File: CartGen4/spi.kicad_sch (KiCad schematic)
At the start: 11 parts, among them J1 MEM2080-00-128-00-A, U10 IS25WP080D-JNLE, U11 DS1391U-33+, Y1 FC-135R 32.7680KA-E5

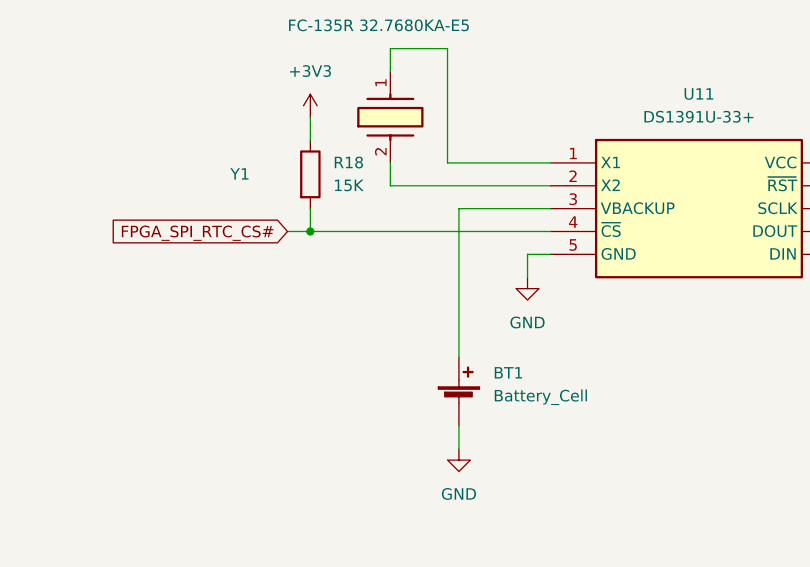
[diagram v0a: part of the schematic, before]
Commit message: Wired SPI bus
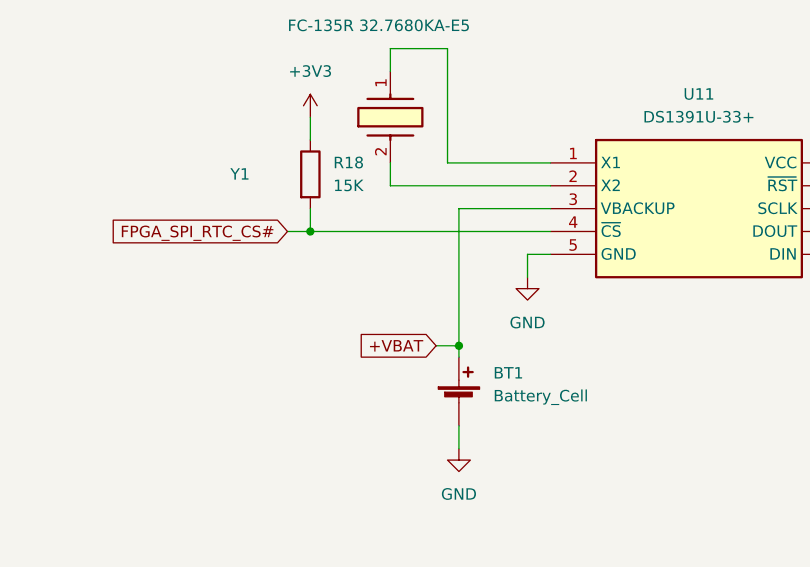
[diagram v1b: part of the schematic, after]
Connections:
- net +VBAT: now reaches BT1.1 (+), U11.3 (VBACKUP)
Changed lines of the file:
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@@
   (junction (at 66.04 125.73) (diameter 0) (color 0 0 0 0)
+  )
+  (junction (at 184.15 88.9) (diameter 0) (color 0 0 0 0)
   )
   (junction (at 252.73 68.58) (diameter 0) (color 0 0 0 0)
@@
     (stroke (width 0) (type default) (color 0 0 0 0))
   )
-  (wire (pts (xy 184.15 90.17) (xy 184.15 73.66))
+  (wire (pts (xy 184.15 90.17) (xy 184.15 88.9))
     (stroke (width 0) (type default) (color 0 0 0 0))
   )
@@
     (stroke (width 0) (type default) (color 0 0 0 0))
   )
+  (wire (pts (xy 184.15 88.9) (xy 184.15 73.66))
+    (stroke (width 0) (type default) (color 0 0 0 0))
+  )
   (wire (pts (xy 118.11 69.85) (xy 118.11 67.31))
+    (stroke (width 0) (type default) (color 0 0 0 0))
+  )
+  (wire (pts (xy 181.61 88.9) (xy 184.15 88.9))
     (stroke (width 0) (type default) (color 0 0 0 0))
   )
@@
       (effects (font (size 1.27 1.27)) (justify right) hide)
     )
+  )
+  (global_label "+VBAT" (shape input) (at 181.61 88.9 180) (fields_autoplaced)
+    (effects (font (size 1.27 1.27)) (justify right))
+    (property "Intersheet References" "${INTERSHEET_REFS}" (id 0) (at 173.2098 88.8206 0)
+      (effects (font (size 1.27 1.27)) (justify right) hide)
+    )

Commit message: Updated field information
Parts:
- BT1: MFN (none) -> Keystone Electronics; MFP (none) -> 2894; Notes Battery is utilised and maintained by the DS1391U-33+ RTC. -> Battery is utilised and maintained by the DS1391U-33+ RTC. 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
- C33, C34, C35: Package ID (none) -> 0402
- J1: Notes (none) -> SD card connector; Source (none) -> SPEC
- R16, R17, R18: Notes (none) -> Pullup resistor for ensuring that slave is not selecting du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; Package ID (none) -> 0402
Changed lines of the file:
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@@
+      (effects (font (size 1.27 1.27)) hide)
+    )
+    (property "Notes" "Pullup resistor for ensuring that slave is not selecting during startup" (id 7) (at 167.64 69.85 0)
+      (effects (font (size 1.27 1.27)) hide)
+    )
+    (property "Description" "~" (id 8) (at 167.64 69.85 0)
+      (effects (font (size 1.27 1.27)) hide)
+    )
+    (property "MFN" "~" (id 9) (at 167.64 69.85 0)
+      (effects (font (size 1.27 1.27)) hide)
+    )
+    (property "MFP" "~" (id 10) (at 167.64 69.85 0)
+      (effects (font (size 1.27 1.27)) hide)
+    )
+    (property "Package ID" "0402" (id 11) (at 167.64 69.85 0)
       (effects (font (size 1.27 1.27)) hide)
     )
@@
     )
     (property "MFP" "MEM2080-00-128-00-A" (id 7) (at 87.63 132.08 0)
+      (effects (font (size 1.27 1.27)) hide)
+    )
+    (property "Notes" "SD card connector" (id 8) (at 87.63 132.08 0)
+      (effects (font (size 1.27 1.27)) hide)
+    )
+    (property "Package ID" "~" (id 9) (at 87.63 132.08 0)
+      (effects (font (size 1.27 1.27)) hide)
+    )
+    (property "Source" "SPEC" (id 10) (at 87.63 132.08 0)
       (effects (font (size 1.27 1.27)) hide)
     )
@@
       (effects (font (size 1.27 1.27)) hide)
     )
+    (property "Description" "~" (id 7) (at 118.11 76.2 0)
+      (effects (font (size 1.27 1.27)) hide)
+    )
+    (property "MFN" "~" (id 8) (at 118.11 76.2 0)
+      (effects (font (size 1.27 1.27)) hide)
+    )
+    (property "MFP" "~" (id 9) (at 118.11 76.2 0)
+      (effects (font (size 1.27 1.27)) hide)
+    )
+    (property "Package ID" "0402" (id 10) (at 118.11 76.2 0)
+      (effects (font (size 1.27 1.27)) hide)
+    )
     (pin "1")
     (pin "2")
@@
     )
     (property "Source" "ANY" (id 6) (at 58.42 132.08 0)
+      (effects (font (size 1.27 1.27)) hide)
+    )
+    (property "Description" "~" (id 7) (at 58.42 132.08 0)
+      (effects (font (size 1.27 1.27)) hide)
+    )
+    (property "MFN" "~" (id 8) (at 58.42 132.08 0)
+      (effects (font (size 1.27 1.27)) hide)
+    )
+    (property "MFP" "~" (id 9) (at 58.42 132.08 0)
+      (effects (font (size 1.27 1.27)) hide)
+    )
+    (property "Package ID" "0402" (id 10) (at 58.42 132.08 0)
       (effects (font (size 1.27 1.27)) hide)
     )
@@
       (effects (font (size 1.27 1.27)) hide)
     )
+    (property "Notes" "Pullup resistor for ensuring that slave is not selecting during startup" (id 7) (at 45.72 139.7 0)
+      (effects (font (size 1.27 1.27)) hide)
+    )
+    (property "Description" "~" (id 8) (at 45.72 139.7 0)
+      (effects (font (size 1.27 1.27)) hide)
+    )
+    (property "MFN" "~" (id 9) (at 45.72 139.7 0)
+      (effects (font (size 1.27 1.27)) hide)
+    )
+    (property "MFP" "~" (id 10) (at 45.72 139.7 0)
+      (effects (font (size 1.27 1.27)) hide)
+    )
+    (property "Package ID" "0402" (id 11) (at 45.72 139.7 0)
+      (effects (font (size 1.27 1.27)) hide)
+    )
     (pin "1")
     (pin "2")
@@
     )
     (property "Source" "ANY" (id 6) (at 252.73 74.93 0)
+      (effects (font (size 1.27 1.27)) hide)
+    )
+    (property "Description" "~" (id 7) (at 252.73 74.93 0)
+      (effects (font (size 1.27 1.27)) hide)
+    )
+    (property "MFN" "~" (id 8) (at 252.73 74.93 0)
+      (effects (font (size 1.27 1.27)) hide)
+    )
+    (property "MFP" "~" (id 9) (at 252.73 74.93 0)
+      (effects (font (size 1.27 1.27)) hide)
+    )
+    (property "Package ID" "0402" (id 10) (at 252.73 74.93 0)
       (effects (font (size 1.27 1.27)) hide)
     )
@@
       (effects (font (size 1.27 1.27)) hide)
     )
-    (property "Datasheet" "~" (id 3) (at 184.15 93.726 90)
+    (property "Datasheet" "https://nl.mouser.com/datasheet/2/215/Keystone_Electronics_04082019_2894-1551346.pdf" (id 3) (at 184.15 93.726 90)
       (effects (font (size 1.27 1.27)) hide)
     )
@@
       (effects (font (size 1.27 1.27)) hide)
     )
-    (property "Notes" "Battery is utilised and maintained by the DS1391U-33+ RTC." (id 5) (at 184.15 95.25 0)
+    (property "Notes" "Battery is utilised and maintained by the DS1391U-33+ RTC. Be sure to disable charging when using non-rechargable batteries." (id 5) (at 184.15 95.25 0)
       (effects (font (size 1.27 1.27)) hide)
     )
     (property "Source" "SPEC" (id 6) (at 184.15 95.25 0)
+      (effects (font (size 1.27 1.27)) hide)
+    )
+    (property "Description" "CR2025 battery holder" (id 7) (at 184.15 95.25 0)
+      (effects (font (size 1.27 1.27)) hide)
+    )
+    (property "MFN" "Keystone Electronics" (id 8) (at 184.15 95.25 0)
+      (effects (font (size 1.27 1.27)) hide)
+    )
+    (property "MFP" "2894" (id 9) (at 184.15 95.25 0)
+      (effects (font (size 1.27 1.27)) hide)
+    )
+    (property "Package ID" "~" (id 10) (at 184.15 95.25 0)
       (effects (font (size 1.27 1.27)) hide)
     )
@@
       (effects (font (size 1.27 1.27)) hide)
     )
+    (property "Notes" "Pullup resistor for ensuring that slave is not selecting during startup" (id 7) (at 54.61 63.5 0)
+      (effects (font (size 1.27 1.27)) hide)
+    )
+    (property "Description" "~" (id 8) (at 54.61 63.5 0)
+      (effects (font (size 1.27 1.27)) hide)
+    )
+    (property "MFN" "~" (id 9) (at 54.61 63.5 0)
+      (effects (font (size 1.27 1.27)) hide)
+    )
+    (property "MFP" "~" (id 10) (at 54.61 63.5 0)
+      (effects (font (size 1.27 1.27)) hide)
+    )
+    (property "Package ID" "0402" (id 11) (at 54.61 63.5 0)
+      (effects (font (size 1.27 1.27)) hide)
+    )

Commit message: Updated some component fields
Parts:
- BT1: Supplier suggestion (none) -> https://nl.mouser.com/ProductDetail/Keystone-Electronics/28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
- C33, C34, C35: Supplier suggestion (none) -> https://nl.mouser.com/ProductDetail/Murata-Electronics/GRM1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; Tolerance (none) -> 20%; Voltage (none) -> 3V3
- J1: Supplier suggestion (none) -> https://nl.mouser.com/ProductDetail/GCT/MEM2080-00-128-00-A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
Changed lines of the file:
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@@
+      (effects (font (size 1.27 1.27)) hide)
+    )
+    (property "Supplier suggestion" "https://nl.mouser.com/ProductDetail/GCT/MEM2080-00-128-00-A?qs=vvQtp7zwQdPJXzpf1SnYug%3D%3D" (id 11) (at 87.63 132.08 0)
       (effects (font (size 1.27 1.27)) hide)
     )
@@
       (effects (font (size 1.27 1.27)) hide)
     )
+    (property "Supplier suggestion" "https://nl.mouser.com/ProductDetail/Murata-Electronics/GRM155R61C104KA88J?qs=sGAEpiMZZMsh%252B1woXyUXj8YF%2FGivH5Kx4uStnYyl8jU%3D" (id 11) (at 118.11 76.2 0)
+      (effects (font (size 1.27 1.27)) hide)
+    )
+    (property "Tolerance" "20%" (id 12) (at 118.11 76.2 0)
+      (effects (font (size 1.27 1.27)) hide)
+    )
+    (property "Voltage" "3V3" (id 13) (at 118.11 76.2 0)
+      (effects (font (size 1.27 1.27)) hide)
+    )
     (pin "1")
     (pin "2")
@@
     )
     (property "Package ID" "0402" (id 10) (at 58.42 132.08 0)
+      (effects (font (size 1.27 1.27)) hide)
+    )
+    (property "Supplier suggestion" "https://nl.mouser.com/ProductDetail/Murata-Electronics/GRM155R61C104KA88J?qs=sGAEpiMZZMsh%252B1woXyUXj8YF%2FGivH5Kx4uStnYyl8jU%3D" (id 11) (at 58.42 132.08 0)
+      (effects (font (size 1.27 1.27)) hide)
+    )
+    (property "Tolerance" "20%" (id 12) (at 58.42 132.08 0)
+      (effects (font (size 1.27 1.27)) hide)
+    )
+    (property "Voltage" "3V3" (id 13) (at 58.42 132.08 0)
       (effects (font (size 1.27 1.27)) hide)
     )
@@
     )
     (property "Package ID" "0402" (id 10) (at 252.73 74.93 0)
+      (effects (font (size 1.27 1.27)) hide)
+    )
+    (property "Supplier suggestion" "https://nl.mouser.com/ProductDetail/Murata-Electronics/GRM155R61C104KA88J?qs=sGAEpiMZZMsh%252B1woXyUXj8YF%2FGivH5Kx4uStnYyl8jU%3D" (id 11) (at 252.73 74.93 0)
+      (effects (font (size 1.27 1.27)) hide)
+    )
+    (property "Tolerance" "20%" (id 12) (at 252.73 74.93 0)
+      (effects (font (size 1.27 1.27)) hide)
+    )
+    (property "Voltage" "3V3" (id 13) (at 252.73 74.93 0)
       (effects (font (size 1.27 1.27)) hide)
     )
@@
       (effects (font (size 1.27 1.27)) hide)
     )
+    (property "Supplier suggestion" "https://nl.mouser.com/ProductDetail/Keystone-Electronics/2894?qs=u16ybLDytRb94n%2F3dXyVLQ%3D%3D" (id 11) (at 184.15 95.25 0)
+      (effects (font (size 1.27 1.27)) hide)
+    )

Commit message: Added missing recommendations
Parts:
- R16, R17, R18: Supplier suggestion (none) -> https://nl.mouser.com/ProductDetail/Kamaya/RMC1-16S-153JTH?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
- U10: Supplier suggestion (none) -> https://nl.mouser.com/ProductDetail/ISSI/IS25WP080D-JNLE?qs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
- U11: Supplier suggestion (none) -> https://nl.mouser.com/ProductDetail/Analog-Devices-Maxim-In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
- Y1: Supplier suggestion (none) -> https://nl.mouser.com/ProductDetail/Epson-Timing/FC-135R-32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
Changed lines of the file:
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@@
+      (effects (font (size 1.27 1.27)) hide)
+    )
+    (property "Supplier suggestion" "https://nl.mouser.com/ProductDetail/Kamaya/RMC1-16S-153JTH?qs=sGAEpiMZZMvdGkrng054t%252BjmMOhbS7JJ11bN0iqZRdOn%2Fu9rqH1%2FEw%3D%3D" (id 12) (at 167.64 69.85 0)
       (effects (font (size 1.27 1.27)) hide)
     )
@@
       (effects (font (size 1.27 1.27)) hide)
     )
+    (property "Supplier suggestion" "https://nl.mouser.com/ProductDetail/Epson-Timing/FC-135R-32.7680KA-E5?qs=%252B6g0mu59x7IiWErQB8ij2w%3D%3D" (id 18) (at 176.53 68.58 0)
+      (effects (font (size 1.27 1.27)) hide)
+    )
     (pin "1")
     (pin "2")
@@
     )
     (property "Package ID" "0402" (id 11) (at 45.72 139.7 0)
+      (effects (font (size 1.27 1.27)) hide)
+    )
+    (property "Supplier suggestion" "https://nl.mouser.com/ProductDetail/Kamaya/RMC1-16S-153JTH?qs=sGAEpiMZZMvdGkrng054t%252BjmMOhbS7JJ11bN0iqZRdOn%2Fu9rqH1%2FEw%3D%3D" (id 12) (at 45.72 139.7 0)
       (effects (font (size 1.27 1.27)) hide)
     )
@@
     )
     (property "Package ID" "SOIC-8" (id 10) (at 67.31 69.85 0)
+      (effects (font (size 1.27 1.27)) hide)
+    )
+    (property "Supplier suggestion" "https://nl.mouser.com/ProductDetail/ISSI/IS25WP080D-JNLE?qs=pif5%252B9MYt0UdCheWbE26RA%3D%3D" (id 11) (at 67.31 69.85 0)
       (effects (font (size 1.27 1.27)) hide)
     )
@@
     )
     (property "Source" "SPEC" (id 10) (at 194.31 68.58 0)
+      (effects (font (size 1.27 1.27)) hide)
+    )
+    (property "Supplier suggestion" "https://nl.mouser.com/ProductDetail/Analog-Devices-Maxim-Integrated/DS1391U-33%2b?qs=0Y9aZN%252BMVCVmg1eZRkyk7Q%3D%3D" (id 11) (at 194.31 68.58 0)
       (effects (font (size 1.27 1.27)) hide)
     )
@@
       (effects (font (size 1.27 1.27)) hide)
     )
+    (property "Supplier suggestion" "https://nl.mouser.com/ProductDetail/Kamaya/RMC1-16S-153JTH?qs=sGAEpiMZZMvdGkrng054t%252BjmMOhbS7JJ11bN0iqZRdOn%2Fu9rqH1%2FEw%3D%3D" (id 12) (at 54.61 63.5 0)
+      (effects (font (size 1.27 1.27)) hide)
+    )

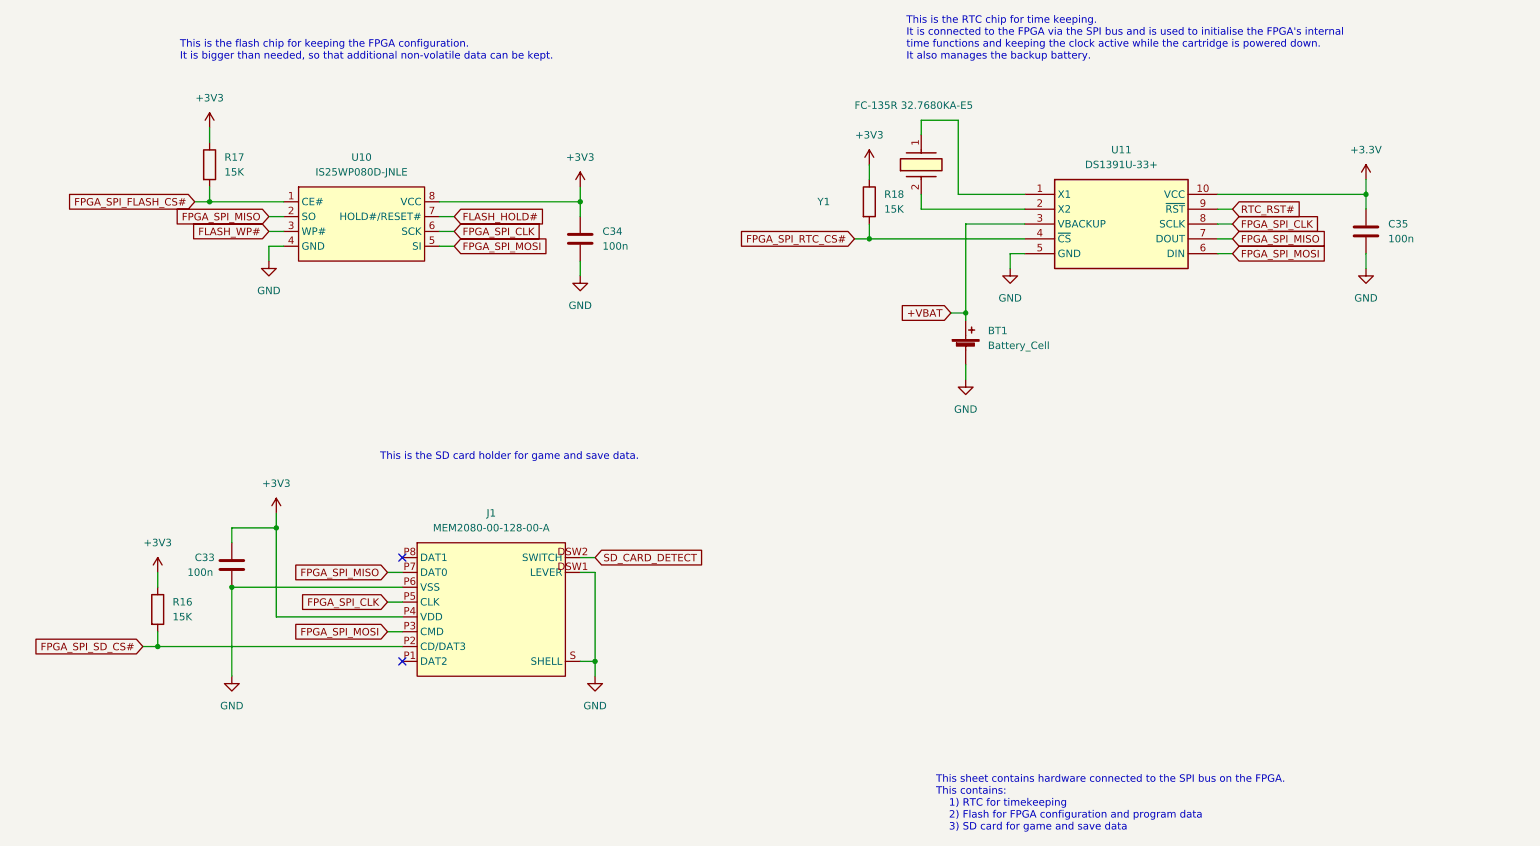
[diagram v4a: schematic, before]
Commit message: Reassigned RD geographically
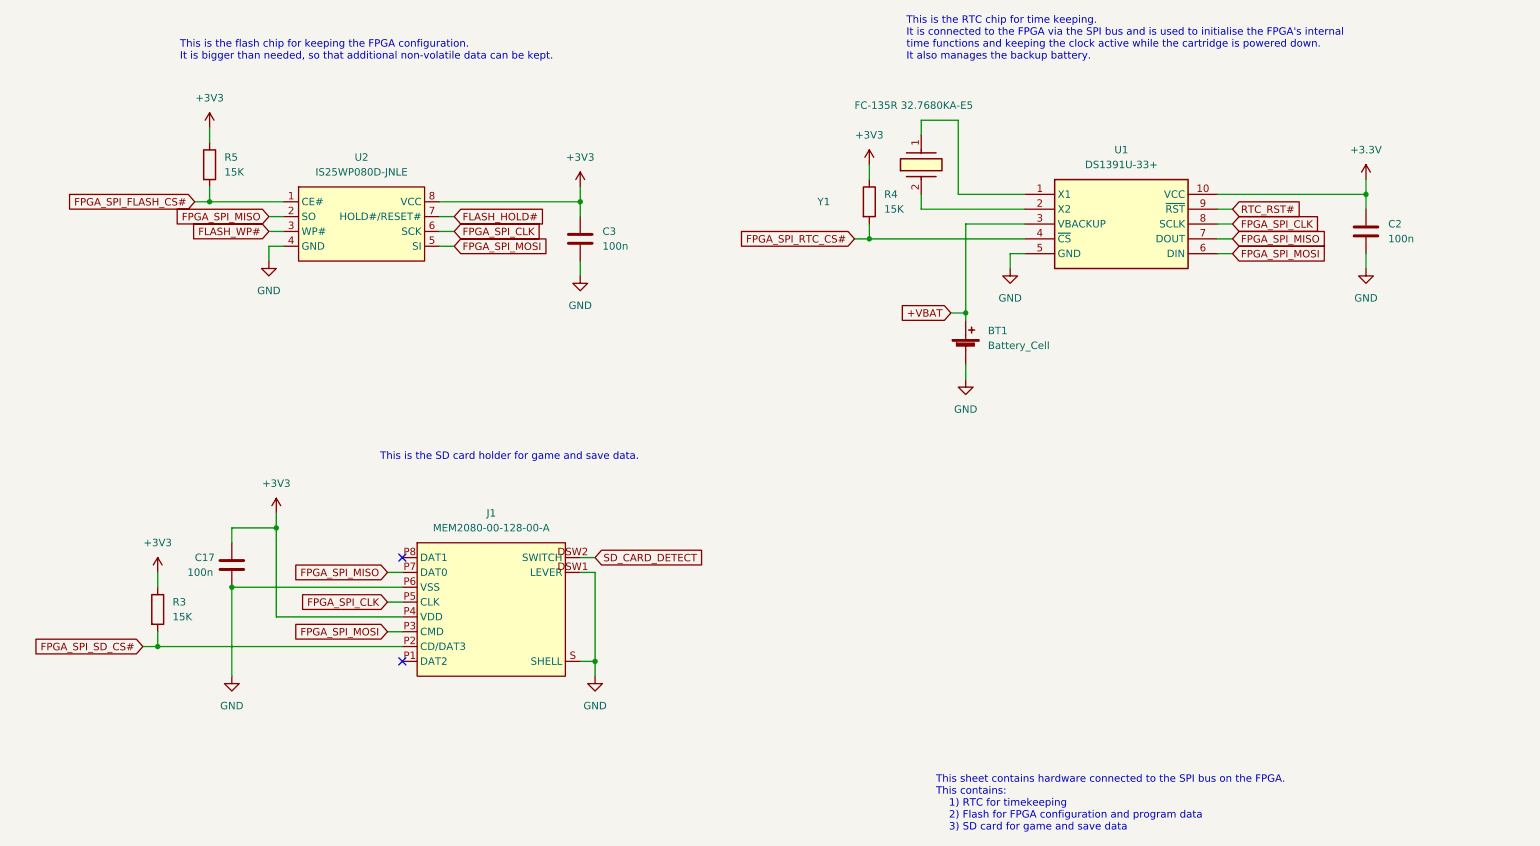
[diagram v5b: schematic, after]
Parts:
- renumbered C33 to C17, C35 to C2, C34 to C3, R16 to R3, R18 to R4, R17 to R5, U11 to U1, U10 to U2
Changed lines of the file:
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@@
   (symbol (lib_id "Device:R") (at 167.64 69.85 0) (unit 1)
     (in_bom yes) (on_board yes) (fields_autoplaced)
-    (property "Reference" "R18" (id 0) (at 170.18 68.5799 0)
+    (property "Reference" "R4" (id 0) (at 170.18 68.5799 0)
       (effects (font (size 1.27 1.27)) (justify left))
     )
@@
   (symbol (lib_id "Device:C") (at 118.11 76.2 0) (unit 1)
     (in_bom yes) (on_board yes) (fields_autoplaced)
-    (property "Reference" "C34" (id 0) (at 121.92 74.9299 0)
+    (property "Reference" "C3" (id 0) (at 121.92 74.9299 0)
       (effects (font (size 1.27 1.27)) (justify left))
     )
@@
   (symbol (lib_id "Device:C") (at 58.42 132.08 0) (unit 1)
     (in_bom yes) (on_board yes)
-    (property "Reference" "C33" (id 0) (at 52.07 130.81 0)
+    (property "Reference" "C17" (id 0) (at 52.07 130.81 0)
       (effects (font (size 1.27 1.27)) (justify left))
     )
@@
   (symbol (lib_id "Device:R") (at 45.72 139.7 0) (unit 1)
     (in_bom yes) (on_board yes) (fields_autoplaced)
-    (property "Reference" "R16" (id 0) (at 48.26 138.4299 0)
+    (property "Reference" "R3" (id 0) (at 48.26 138.4299 0)
       (effects (font (size 1.27 1.27)) (justify left))
     )
@@
   (symbol (lib_id "Device:C") (at 252.73 74.93 0) (unit 1)
     (in_bom yes) (on_board yes) (fields_autoplaced)
-    (property "Reference" "C35" (id 0) (at 256.54 73.6599 0)
+    (property "Reference" "C2" (id 0) (at 256.54 73.6599 0)
       (effects (font (size 1.27 1.27)) (justify left))
     )
@@
   (symbol (lib_id "SamacSys_Parts:IS25WP080D-JNLE") (at 67.31 69.85 0) (unit 1)
     (in_bom yes) (on_board yes) (fields_autoplaced)
-    (property "Reference" "U10" (id 0) (at 80.645 62.23 0))
+    (property "Reference" "U2" (id 0) (at 80.645 62.23 0))
     (property "Value" "IS25WP080D-JNLE" (id 1) (at 80.645 64.77 0))
     (property "Footprint" "SamacSys_Parts:NE555DR" (id 2) (at 67.31 69.85 0)
@@
   (symbol (lib_id "SamacSys_Parts:DS1391U-33+") (at 194.31 68.58 0) (unit 1)
     (in_bom yes) (on_board yes) (fields_autoplaced)
-    (property "Reference" "U11" (id 0) (at 210.82 60.96 0))
+    (property "Reference" "U1" (id 0) (at 210.82 60.96 0))
     (property "Value" "DS1391U-33+" (id 1) (at 210.82 63.5 0))
     (property "Footprint" "SamacSys_Parts:SOP50P490X110-10N" (id 2) (at 194.31 68.58 0)
@@
   (symbol (lib_id "Device:R") (at 54.61 63.5 0) (unit 1)
     (in_bom yes) (on_board yes) (fields_autoplaced)
-    (property "Reference" "R17" (id 0) (at 57.15 62.2299 0)
-      (effects (font (size 1.27 1.27)) (justify left))
-    )
+    (property "Reference" "R5" (id 0) (at 57.15 62.2299 0)
+      (effects (font (size 1.27 1.27)) (justify left))
+    )
